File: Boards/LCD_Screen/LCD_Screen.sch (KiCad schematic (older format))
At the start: 31 parts, among them J1 MicroFit_VT_4, U1 MCP25625-x-SS, U2 Raspberry_Pi_Zero, U3 TPS563231, Y1 Crystal_SMD

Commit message: Fixing errors in LCD buck
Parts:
- C10: symbol LCD_Screen-rescue:C_10uF-footprints-Buck_HighCurrent-rescue -> formula:C_10uF
- C11: symbol LCD_Screen-rescue:C_22uF-footprints-Buck_HighCurrent-rescue -> formula:C_22uF
- C12: footprint Capacitor_SMD:C_1812_4532Metric -> footprints:Fuse_1812; symbol LCD_Screen-rescue:C_33uF-footprints-Buck_HighCurrent-rescue -> formula:C_33uF; MFN C4532X7R1C336M250KC -> DK
- C5, C8: symbol LCD_Screen-rescue:C_0.1uF_0603-footprints-Buck_HighCurrent-rescue -> formula:C_0.1uF_0603
- C6, C7: symbol LCD_Screen-rescue:C_10uF_25V-footprints-Buck_HighCurrent-rescue -> formula:C_10uF_25V
- C9: symbol LCD_Screen-rescue:C_100nF-footprints-Buck_HighCurrent-rescue -> formula:C_100nF
- D1: symbol LCD_Screen-rescue:D_Zener_18V-footprints-Buck_HighCurrent-rescue -> formula:D_Zener_18V
- D2, D3: symbol LCD_Screen-rescue:LED_0805-footprints-Buck_HighCurrent-rescue -> formula:LED_0805
- F1: footprint Fuse:Fuse_1812_4532Metric -> footprints:Fuse_1812_4532Metric; symbol LCD_Screen-rescue:F_2.6A_16V-footprints-Buck_HighCurrent-rescue -> formula:F_2.6A_16V
- L1: symbol LCD_Screen-rescue:IHLP2020BZER4R7M11-footprints-Buck_HighCurrent-rescue -> formula:IHLP2020BZER4R7M11
- R1: symbol LCD_Screen-rescue:R_200-footprints-Buck_HighCurrent-rescue -> formula:R_1K; MPN RMCF0805JT200RCT-ND -> RNCP0805FTD1K00CT-ND; PurchasingLink https://www.digikey.com/products/en?keywords=RMCF0805JT200R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 -> https://www.digikey.com/products/en?keywords=RNCP0805FTD1K0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
- R4: symbol LCD_Screen-rescue:R_10K-footprints-Buck_HighCurrent-rescue -> formula:R_10K
- R5: symbol LCD_Screen-rescue:R_51.1K-footprints-Buck_HighCurrent-rescue -> formula:R_51.1K
- R6: symbol LCD_Screen-rescue:R_22K-footprints-Buck_HighCurrent-rescue -> formula:R_22K
- R7: footprint footprints:R_0603_1608Metric -> footprints:R_0805_OEM; symbol LCD_Screen-rescue:R_1-footprints-Buck_HighCurrent-rescue -> formula:R_1
- R8: symbol LCD_Screen-rescue:R_0_2512-footprints-Buck_HighCurrent-rescue -> formula:R_0_2512
- R9: symbol LCD_Screen-rescue:R_200-footprints-Buck_HighCurrent-rescue -> formula:R_200
- U2: symbol Connector_Generic:Conn_02x20_Odd_Even -> formula:Raspberry_Pi_Zero
- U3: symbol LCD_Screen-rescue:TPS563231-footprints-Buck_HighCurrent-rescue -> formula:TPS563231
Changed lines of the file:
@@
 EESchema Schematic File Version 4
 LIBS:LCD_Screen-cache
-EELAYER 30 0
+EELAYER 26 0
 EELAYER END
 $Descr A4 11693 8268
@@
 F 1 "PWR_FLAG" H 10350 6074 50  0000 C CNN
 F 2 "" H 10350 5900 50  0001 C CNN
-F 3 "~" H 10350 5900 50  0001 C CNN
+F 3 "" H 10350 5900 50  0001 C CNN
 	1    10350 5900
 	1    0    0    -1
@@
 F 1 "PWR_FLAG" H 9950 6074 50  0000 C CNN
 F 2 "" H 9950 5900 50  0001 C CNN
-F 3 "~" H 9950 5900 50  0001 C CNN
+F 3 "" H 9950 5900 50  0001 C CNN
 	1    9950 5900
 	1    0    0    -1
@@
 F 1 "PWR_FLAG" H 9550 6074 50  0000 C CNN
 F 2 "" H 9550 5900 50  0001 C CNN
-F 3 "~" H 9550 5900 50  0001 C CNN
+F 3 "" H 9550 5900 50  0001 C CNN
 	1    9550 5900
 	1    0    0    -1
@@
 MISO
 $Comp
-L Connector_Generic:Conn_02x20_Odd_Even U2
+L formula:Raspberry_Pi_Zero U2
 U 1 1 5DCDFF6E
 P 6450 5900
@@
 F 1 "Raspberry_Pi_Zero" H 6500 6926 50  0000 C CNN
 F 2 "footprints:PinHeader_2x20_P2.54mm_Vertical" H 6450 5900 50  0001 C CNN
-F 3 "~" H 6450 5900 50  0001 C CNN
+F 3 "" H 6450 5900 50  0001 C CNN
 	1    6450 5900
 	1    0    0    -1
@@
 F 1 "MCP25625-x-SS" H 2400 4528 50  0000 C CNN
 F 2 "Package_SO:SSOP-28_5.3x10.2mm_P0.65mm" H 2500 5700 50  0001 C CNN
-F 3 "http://ww1.microchip.com/downloads/en/DeviceDoc/20005282B.pdf" H 2400 6600 50  0001 C CNN
+F 3 "" H 2400 6600 50  0001 C CNN
 	1    2400 6000
 	1    0    0    -1
@@
 	2750 1500 2250 1500
 $Comp
-L LCD_Screen-rescue:C_0.1uF_0603-footprints-Buck_HighCurrent-rescue C5
+L formula:C_0.1uF_0603 C5
 U 1 1 5DD296FF
 P 2750 1750
@@
 $EndComp
 $Comp
-L LCD_Screen-rescue:R_200-footprints-Buck_HighCurrent-rescue R1
+L formula:R_1K R1
 U 1 1 5DD24939
 P 2250 1750
@@
 F 1 "R_1K" V 2350 1650 50  0000 L CNN
 F 2 "footprints:R_0805_OEM" H 2180 1750 50  0001 C CNN
-F 3 "https://www.seielect.com/Catalog/SEI-RMCF_RMCP.pdf" H 2330 1750 50  0001 C CNN
+F 3 "https://www.seielect.com/Catalog/SEI-rncp.pdf" H 2330 1750 50  0001 C CNN
 F 4 "DK" H 2250 1750 60  0001 C CNN "MFN"
-F 5 "RMCF0805JT200RCT-ND" H 2250 1750 60  0001 C CNN "MPN"
-F 6 "https://www.digikey.com/products/en?keywords=RMCF0805JT200RCT-ND" H 2730 2150 60  0001 C CNN "PurchasingLink"
+F 5 "RNCP0805FTD1K00CT-ND" H 2250 1750 60  0001 C CNN "MPN"
+F 6 "https://www.digikey.com/products/en?keywords=RNCP0805FTD1K00CT-ND" H 2730 2150 60  0001 C CNN "PurchasingLink"
 	1    2250 1750
 	1    0    0    -1
 $EndComp
 $Comp
-L LCD_Screen-rescue:LED_0805-footprints-Buck_HighCurrent-rescue D2
+L formula:LED_0805 D2
 U 1 1 5DD25EAF
 P 2250 2100
@@
 	2250 1900 2250 1950
 $Comp
-L LCD_Screen-rescue:D_Zener_18V-footprints-Buck_HighCurrent-rescue D1
+L formula:D_Zener_18V D1
 U 1 1 5DD288D2
 P 1700 2100
@@
 	1700 1950 1700 1500
 $Comp
-L LCD_Screen-rescue:F_2.6A_16V-footprints-Buck_HighCurrent-rescue F1
+L formula:F_2.6A_16V F1
 U 1 1 5DD2DCBD
 P 1950 1500
-F 0 "F1" V 1850 1500 50  0000 C CNN
-F 1 "F_2.6A_16V" V 2050 1500 50  0000 C CNN
-F 2 "Fuse:Fuse_1812_4532Metric" H 1950 1500 50  0001 C CNN
-F 3 "https://www.belfuse.com/resources/CircuitProtection/datasheets/0ZCG%20Nov2016.pdf" H 1950 1500 50  0001 C CNN
+F 0 "F1" H 1950 1600 50  0000 C CNN
+F 1 "F_2.6A_16V" H 1950 1400 50  0000 C CNN
+F 2 "footprints:Fuse_1812_4532Metric" H 1950 1500 50  0001 C CNN
+F 3 "" H 1950 1500 50  0001 C CNN
 F 4 "https://www.digikey.com/product-detail/en/bel-fuse-inc/0ZCG0260BF2B/507-1780-6-ND/4156287" H 2010 1409 50  0001 L CNN "Digikey"
 	1    1950 1500
-	0    1    1    0
+	1    0    0    -1
 $EndComp
 Wire Wire Line
@@
 	3550 1600 3550 1500
 $Comp
-L LCD_Screen-rescue:C_10uF_25V-footprints-Buck_HighCurrent-rescue C7
+L formula:C_10uF_25V C7
 U 1 1 5DD2E6F4
 P 3550 1750
@@
 $EndComp
 $Comp
-L LCD_Screen-rescue:C_10uF_25V-footprints-Buck_HighCurrent-rescue C6
+L formula:C_10uF_25V C6
 U 1 1 5DD2D3E3
 P 3150 1750
@@
 $EndComp
 $Comp
-L LCD_Screen-rescue:C_0.1uF_0603-footprints-Buck_HighCurrent-rescue C8
+L formula:C_0.1uF_0603 C8
 U 1 1 5DD434B0
 P 5250 1450
@@
 	5700 1450 5900 1450
 $Comp
-L LCD_Screen-rescue:IHLP2020BZER4R7M11-footprints-Buck_HighCurrent-rescue L1
+L formula:IHLP2020BZER4R7M11 L1
 U 1 1 5DD494D5
-P 5900 1450
-F 0 "L1" H 6200 1750 60  0000 C CNN
-F 1 "L_4.7uH_3.2A" H 6200 1650 60  0000 C CNN
-F 2 "footprints:IHLP2020BZER4R7M11" H 6175 1165 60  0001 C CNN
-F 3 "http://www.vishay.com/docs/34261/ihlp2020bz11.pdf" H 5900 1450 60  0001 C CNN
-F 4 "https://www.digikey.com/product-detail/en/vishay-dale/IHLP2020BZER4R7M11/541-1222-1-ND/2025112" H 5900 1450 50  0001 C CNN "Vendor Link"
-	1    5900 1450
-	1    0    0    -1
-$EndComp
-$Comp
-L LCD_Screen-rescue:C_22uF-footprints-Buck_HighCurrent-rescue C11
+P 6200 1450
+F 0 "L1" H 6500 1750 60  0000 C CNN
+F 1 "L_4.7uH_3.2A" H 6500 1650 60  0000 C CNN
+F 2 "footprints:IHLP2020BZER4R7M11" H 6475 1165 60  0001 C CNN
+F 3 "" H 6200 1450 60  0001 C CNN
+F 4 "https://www.digikey.com/product-detail/en/vishay-dale/IHLP2020BZER4R7M11/541-1222-1-ND/2025112" H 6200 1450 50  0001 C CNN "Vendor Link"
+	1    6200 1450
+	1    0    0    -1
+$EndComp
+$Comp
+L formula:C_22uF C11
 U 1 1 5DD4C422
 P 7150 1700
@@
 $EndComp
 $Comp
-L LCD_Screen-rescue:R_51.1K-footprints-Buck_HighCurrent-rescue R5
+L formula:R_51.1K R5
 U 1 1 5DD4EB26
 P 6550 2450
@@
 $EndComp
 $Comp
-L LCD_Screen-rescue:R_22K-footprints-Buck_HighCurrent-rescue R6
+L formula:R_22K R6
 U 1 1 5DD4F8B6
 P 6900 2450
@@
 	5600 2450 5600 2500
 $Comp
-L LCD_Screen-rescue:R_0_2512-footprints-Buck_HighCurrent-rescue R8
+L formula:R_0_2512 R8
 U 1 1 5DD64EC7
 P 8700 1450
@@
 	9100 1450 9100 1300
 $Comp
-L LCD_Screen-rescue:R_200-footprints-Buck_HighCurrent-rescue R9
+L formula:R_200 R9
 U 1 1 5DD69219
 P 9100 1900
@@
 $EndComp
 $Comp
-L LCD_Screen-rescue:LED_0805-footprints-Buck_HighCurrent-rescue D3
+L formula:LED_0805 D3
 U 1 1 5DD69222
 P 9100 2250
@@
 $EndComp
 $Comp
-L LCD_Screen-rescue:C_10uF-footprints-Buck_HighCurrent-rescue C10
+L formula:C_10uF C10
 U 1 1 5DD6B930
 P 6700 1700
@@
 	7050 2450 7450 2450
 $Comp
-L LCD_Screen-rescue:C_100nF-footprints-Buck_HighCurrent-rescue C9
+L formula:C_100nF C9
 U 1 1 5DD78F6F
 P 6450 2800
@@
 $EndComp
 $Comp
-L LCD_Screen-rescue:R_1-footprints-Buck_HighCurrent-rescue R7
+L formula:R_1 R7
 U 1 1 5DD86588
 P 7050 2800
-F 0 "R7" V 7150 2750 50  0000 L CNN
-F 1 "R_1" V 6950 2750 50  0000 L CNN
-F 2 "footprints:R_0603_1608Metric" H 7050 2800 50  0001 C CNN
+F 0 "R7" H 7000 2900 50  0000 L CNN
+F 1 "R_1" H 7000 2700 50  0000 L CNN
+F 2 "footprints:R_0805_OEM" H 7050 2800 50  0001 C CNN
 F 3 "" H 7050 2800 50  0001 C CNN
 F 4 "https://www.digikey.com/product-detail/en/yageo/RC0603FR-071RL/311-1.00HRCT-ND/729789" H 7050 2800 50  0001 C CNN "Link"
 	1    7050 2800
-	0    -1   -1   0
-$EndComp
-$Comp
-L LCD_Screen-rescue:TPS563231-footprints-Buck_HighCurrent-rescue U3
+	1    0    0    -1
+$EndComp
+$Comp
+L formula:TPS563231 U3
 U 1 1 5DD8A4F8
 P 4450 1950
@@
 	6900 2800 6600 2800
 $Comp
-L LCD_Screen-rescue:R_10K-footprints-Buck_HighCurrent-rescue R4
+L formula:R_10K R4
 U 1 1 5DDB9CFE
 P 5600 2650
@@
 $EndComp
 $Comp
-L LCD_Screen-rescue:C_33uF-footprints-Buck_HighCurrent-rescue C12
+L formula:C_33uF C12
 U 1 1 5DD4CD92
 P 7650 1700
 F 0 "C12" H 7600 2050 50  0000 L CNN
 F 1 "C_33uF" V 7800 1550 50  0000 L CNN
-F 2 "Capacitor_SMD:C_1812_4532Metric" H 7700 1300 50  0001 C CNN
-F 3 "https://product.tdk.com/info/en/catalog/datasheets/mlcc_commercial_general_en.pdf" H 7650 2350 50  0001 C CNN
-F 4 "C4532X7R1C336M250KC" H 7700 1200 60  0001 C CNN "MFN"
+F 2 "footprints:Fuse_1812" H 7700 1300 50  0001 C CNN
+F 3 "" H 7650 2350 50  0001 C CNN
+F 4 "DK" H 7700 1200 60  0001 C CNN "MFN"
 F 5 "445-3924-1-ND" H 7650 2050 60  0001 C CNN "MPN"
 F 6 "https://www.digikey.com/product-detail/en/tdk-corporation/C4532X7R1C336M250KC/445-3924-1-ND/1923431" H 7900 2200 60  0001 C CNN "PurchasingLink"
@@
 F 1 "R_120_DNP" H 3420 5105 50  0000 L CNN
 F 2 "footprints:R_0805_OEM" H 2150 5300 50  0001 L CNN
-F 3 "https://www.mouser.com/datasheet/2/315/AOA0000C304-1149620.pdf" H 2150 5600 50  0001 L CNN
+F 3 "" H 2150 5600 50  0001 L CNN
 F 4 "DK" H 3350 5150 60  0001 C CNN "MFN"
 F 5 "667-ERJ-6ENF1200V" H 2150 5400 60  0001 L CNN "MPN"

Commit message: Revert "Begin Layout"
This reverts commit f66e97611986f6cb10e89dffa2fa205961dd2a3d.
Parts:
- removed C10: C_10uF, footprints:C_0805_OEM, symbol formula:C_10uF
- removed C11: C_22uF, footprints:C_1206_OEM, symbol formula:C_22uF
- removed C12: C_33uF, footprints:Fuse_1812, symbol formula:C_33uF
- removed C5: C_0.1uF, footprints:C_0603_1608Metric, symbol formula:C_0.1uF_0603
- removed C6, C7: C_10uF_25V, footprints:C_0805_OEM, symbol formula:C_10uF_25V
- removed C8: C_0.1uF_0603, footprints:C_0603_1608Metric, symbol formula:C_0.1uF_0603
- removed C9: C_100nF, footprints:C_0603_1608Metric, symbol formula:C_100nF
- removed D1: D_Zener_18V, footprints:DO-214AA, symbol formula:D_Zener_18V
- removed D2, D3: LED_0805, footprints:LED_0805_OEM, symbol formula:LED_0805
- removed F1: F_2.6A_16V, footprints:Fuse_1812_4532Metric, symbol formula:F_2.6A_16V
- removed J1: MicroFit_VT_4, footprints:MicroFit_VT_4, symbol formula:MicroFit_VT_4
- removed L1: L_4.7uH_3.2A, footprints:IHLP2020BZER4R7M11, symbol formula:IHLP2020BZER4R7M11
- removed R1: R_1K, footprints:R_0805_OEM, symbol formula:R_1K
- removed R2: R_120_DNP, footprints:R_0805_OEM, symbol formula:R_120_DNP
- removed R4: R_10K, footprints:R_0805_OEM, symbol formula:R_10K
- removed R5: R_51.1K, footprints:R_0805_OEM, symbol formula:R_51.1K
- removed R6: R_22K, footprints:R_0805_OEM, symbol formula:R_22K
- removed R7: R_1, footprints:R_0805_OEM, symbol formula:R_1
- removed R8: R_0_2512, footprints:R_2512_OEM, symbol formula:R_0_2512
- removed R9: R_200, footprints:R_0805_OEM, symbol formula:R_200
- removed U3: TPS563231, footprints:SOT-563, symbol formula:TPS563231
- added C1, C101, C103: C_0.1uF, footprints:C_0805_OEM, symbol formula:C_0.1uF
- added C102: C_2.2uF, footprints:C_0603_1608Metric, symbol formula:C_2.2uF
- added COUT101: C_22uF, footprints:C_1206_OEM, symbol formula:C_22uF
- added COUT102: C_33uF, footprints:Fuse_1812, symbol formula:C_33uF
- added COUT103: C_47uF, footprints:C_0805_OEM, symbol formula:C_47uF
- added D101: D_Zener_18V, footprints:DO-214AA, symbol formula:D_Zener_18V
- added D102, D103: LED_0805, footprints:LED_0805_OEM, symbol formula:LED_0805
- added F101: F_500mA_16V, footprints:Fuse_1210, symbol formula:F_500mA_16V
- added J1: CONN_02X03, footprints:Pin_Header_Straight_2x03, symbol formula:CONN_02X03
- added L101: L_100uH, footprints:L_100uH, symbol formula:L_100uH
- added R1: R_100, footprints:R_0805_OEM, symbol formula:R_100
- added R101, R105, R2: R_200, footprints:R_0805_OEM, symbol formula:R_200
- added R102: R_25K, footprints:R_0805_OEM, symbol formula:R_25K
- added R103: R_100K, footprints:R_0805_OEM, symbol formula:R_100K
- added R104: R_0_2512, footprints:R_2512_OEM, symbol formula:R_0_2512
- added U1: MCP2561-E_SN, footprints:SOIC-8_3.9x4.9mm_Pitch1.27mm_OEM, symbol formula:MCP2561-E_SN
- added U101: TPS560430YF, footprints:SOT-23-6_OEM, symbol formula:TPS560430YF
- added U?: Raspberry_Pi_Zero, symbol Connector:Raspberry_Pi_2_3
- J?: renamed from U2; value Raspberry_Pi_Zero -> Conn_02x20_Odd_Even; footprint footprints:PinHeader_2x20_P2.54mm_Vertical -> (none); symbol formula:Raspberry_Pi_Zero -> Connector_Generic:Conn_02x20_Odd_Even
- renumbered C4 to C?, C1 to C?, U1 to U?, Y1 to Y?
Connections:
- net labels added: CAN_HI, CAN_LO, CAN_RX, CAN_TX, Chip_Select, RESET, SCLK
- net labels removed: CANH, CANL
- wire segments 115 -> 80
- no-connect marks 42 -> 43
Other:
- note added: "12V Indicator"
- note added: "16M1 PROGRAMMING HEADER\n"
- note added: "5V"
- note added: "5V Indicator"
- note added: "Bootstrap Capacitor\n"
- note added: "CAN TRANSCEIVER\n"
- note added: "Feedback Divider\n"
- note added: "Inductor\n"
- note added: "Input Capacitors\n\n"
- note added: "Output Capacitors\n"
- note added: "Protection\n"
- note added: "VCC Jumper\n"
- note removed: "CAN CONTROLLER WITH INTEGRATED TRANSCEIVER\n"
- note removed: "DNP"
- note removed: "MICROFIT"
- moved on the sheet: C2, C3, C?, R3, U?, Y?

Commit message: Started layout of the LCD board
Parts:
- removed C1: C_0.1uF, footprints:C_0805_OEM, symbol formula:C_0.1uF
- removed J1: CONN_02X03, footprints:Pin_Header_Straight_2x03, symbol formula:CONN_02X03
- removed R1: R_100, footprints:R_0805_OEM, symbol formula:R_100
- removed U1: MCP2561-E_SN, footprints:SOIC-8_3.9x4.9mm_Pitch1.27mm_OEM, symbol formula:MCP2561-E_SN
- removed U?: Raspberry_Pi_Zero, symbol Connector:Raspberry_Pi_2_3
- added J1: Ultrafit_4_RA, footprints:Ultrafit_4_RA, symbol formula:Ultrafit_4_RA
- R2: value R_200 -> R_100
- U2: renamed from J?; value Conn_02x20_Odd_Even -> Raspberry_Pi_Zero
- gave numbers to parts that had none: 4
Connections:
- net labels added: CANH, CANL
- net labels removed: CAN_RX, CAN_TX, Chip_Select, RESET, SCLK
- wire segments 80 -> 84
- no-connect marks 43 -> 42
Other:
- note added: "CAN CONTROLLER WITH INTEGRATED TRANSCEIVER\n"
- note added: "DNP"
- note added: "ULTRAFIT\n"
- note removed: "16M1 PROGRAMMING HEADER\n"
- note removed: "CAN TRANSCEIVER\n"
- moved on the sheet: C1, C101, C102, C103, C2, C3, C4, COUT101, COUT102, COUT103, D101, D102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

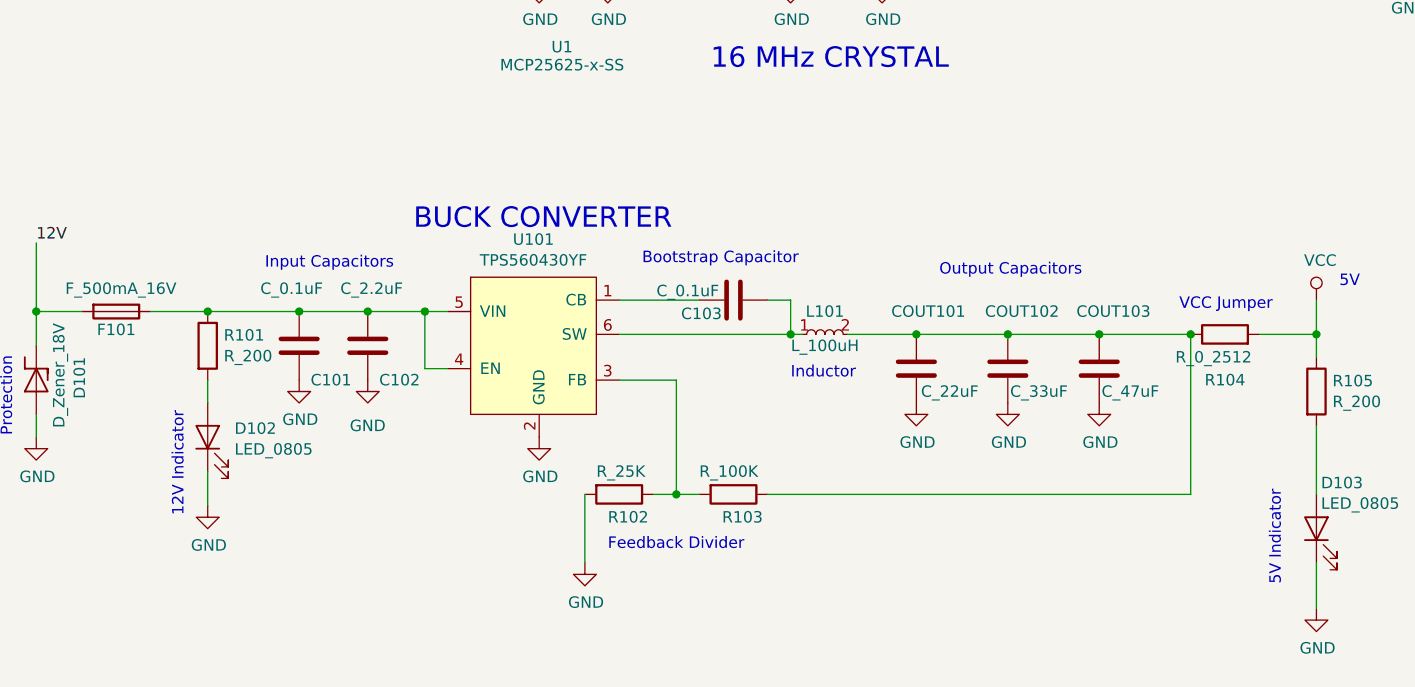
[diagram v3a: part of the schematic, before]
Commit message: finished schematic. only thing needed is the updated buck converter.
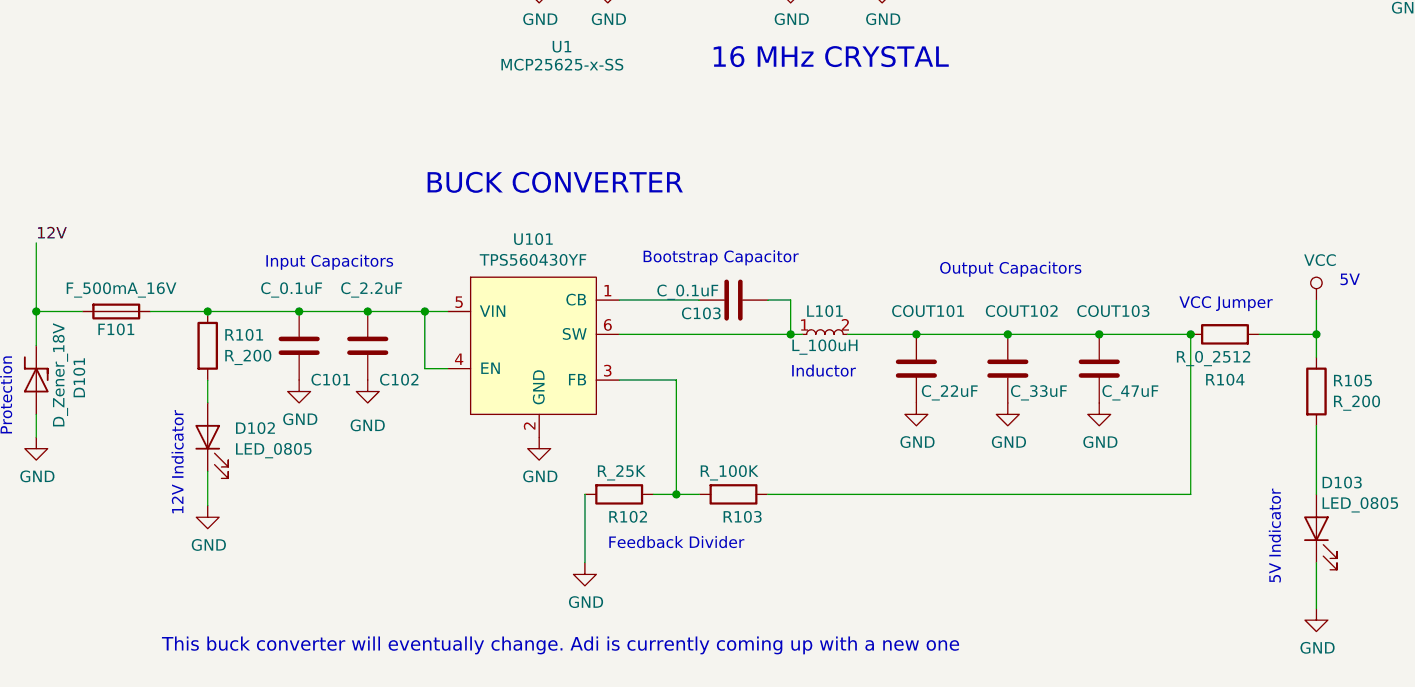
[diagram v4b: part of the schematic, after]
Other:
- note added: "This buck converter will eventually change. Adi is currently coming up with a new one\n"
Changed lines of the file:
@@
 Text Notes 1450 6950 1    50   ~ 0
 12V Indicator
-Text Notes 2450 5700 0    89   ~ 0
+Text Notes 2500 5550 0    89   ~ 0
 BUCK CONVERTER\n
 Text Notes 4100 6350 0    50   ~ 0
@@
 Wire Wire Line
 	10000 4750 10400 4750
-Text Label 10000 4850 0    50   ~ 0
-CANH
-Text Label 10000 4950 0    50   ~ 0
-CANL
 $Comp
 L power:PWR_FLAG #FLG04
@@
 	1    0    0    -1
 $EndComp
+Wire Wire Line
+	10000 4650 10400 4650
+Text Notes 9650 4200 0    89   ~ 0
+ULTRAFIT\n
 $Comp
 L formula:Ultrafit_4_RA J1
@@
 	1    0    0    -1
 $EndComp
-Wire Wire Line
-	10000 4650 10400 4650
-Text Notes 9650 4200 0    89   ~ 0
-ULTRAFIT\n
+Text Label 10000 4850 0    50   ~ 0
+CANH
+Text Label 10000 4950 0    50   ~ 0
+CANL
+Text Notes 1350 7550 0    59   ~ 0
+This buck converter will eventually change. Adi is currently coming up with a new one\n
 $EndSCHEMATC
